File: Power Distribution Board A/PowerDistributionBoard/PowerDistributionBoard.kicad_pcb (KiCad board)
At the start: 2 copper layers, 104.1 x 81.3 mm, 19 parts, among them J0 Battery Input, J1 O1, J2 O2, J3 O3, J4 O4, J5 O5, J6 O6

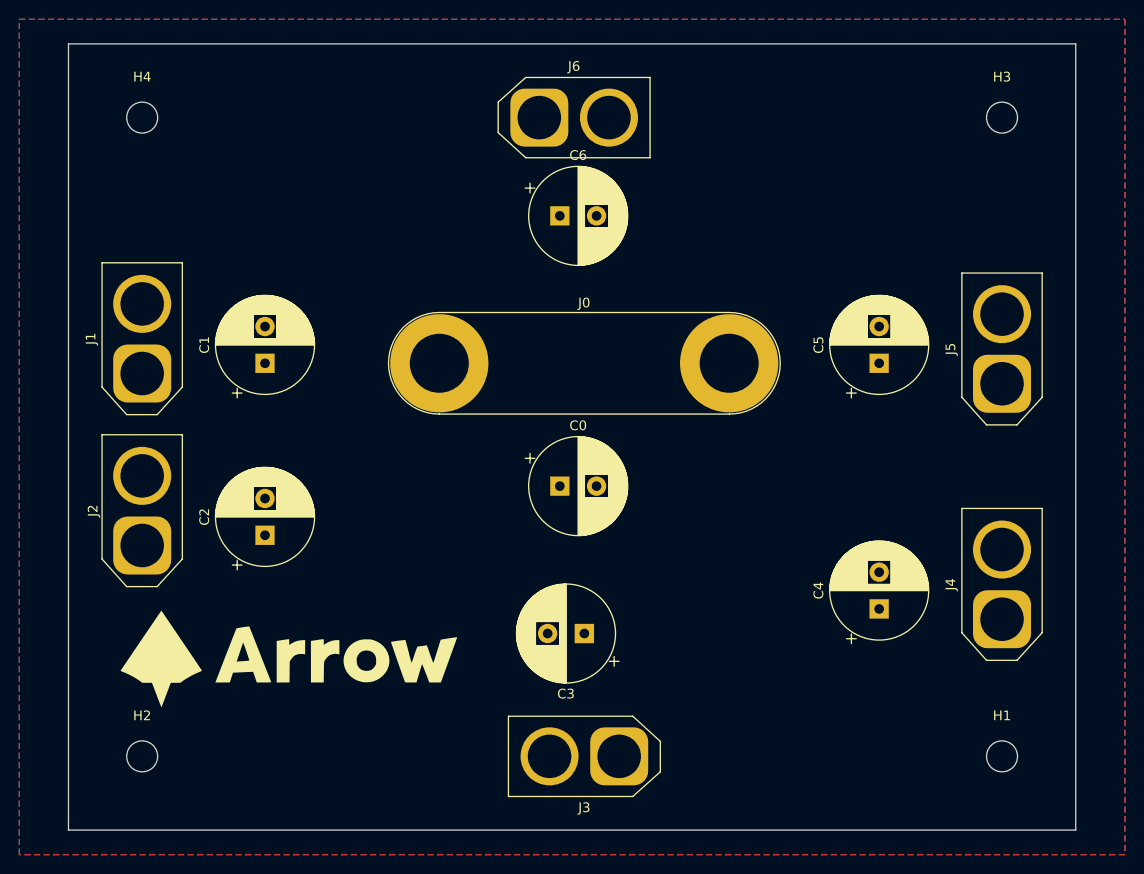
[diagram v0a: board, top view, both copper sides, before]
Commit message: General Update
Board Size Reduced
Colour Scheme Update
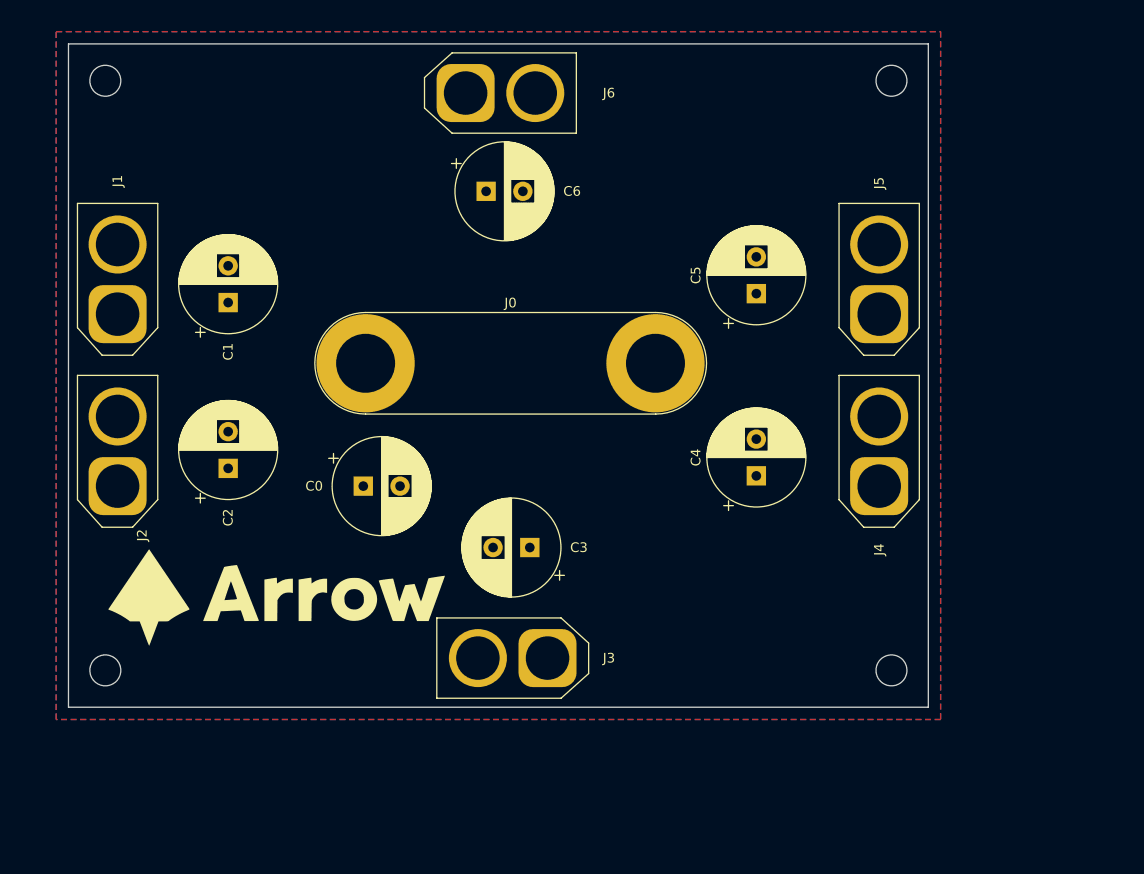
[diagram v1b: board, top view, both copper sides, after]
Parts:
- moved C0 20.3 mm to (78.7, 63.5)
- moved C4 18.7 mm to (119.4, 62.4)
- moved J4 18.7 mm to (132.1, 63.5)
- moved C5 14.6 mm to (119.4, 43.6)
- moved J5 14.6 mm to (132.1, 45.7)
- moved H1 14.5 mm to (133.3, 82.5)
- moved J3 12.6 mm to (97.8, 81.3)
- moved H3 12.0 mm to (133.3, 21.6)
- moved C3 10.5 mm to (96.0, 69.8)
- moved H2 9.67 mm to (52.1, 82.5)
- moved C6 8.03 mm to (91.4, 33.0)
- moved J6 8.03 mm to (89.3, 22.9)
- moved C2 7.89 mm to (64.8, 61.7)
- moved J0 7.62 mm to (79.0, 50.8)
- moved C1 7.34 mm to (64.8, 44.5)
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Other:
- board size 104.1 x 81.3 mm -> 88.9 x 68.6 mm
